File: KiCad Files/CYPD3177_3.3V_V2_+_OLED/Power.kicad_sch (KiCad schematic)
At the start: 36 parts, among them J11 USB_C_Receptacle_USB2.0_14P, J5 Conn_01x02_Pin, J6 Conn_02x02_Counter_Clockwise, J7 Conn_02x02_Counter_Clockwise, U5 TPS62933DRLR, U6 AON7534, U7 AON7534, U8 AP33772S, U9 XC6220B331PR-G

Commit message: changed pcb
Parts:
- removed H2: MountingHole, MountingHole:MountingHole_2.7mm_M2.5_DIN965_Pad_TopBottom, symbol Mechanical:MountingHole
- renumbered C16 to C10, C17 to C11, C18 to C12, C19 to C13, C20 to C14, C21 to C15, C23 to C4, C3 to C5, C24 to C6, C10 to C7, C6 to C8, C11 to C9, D5 to D3, D2 to D4, D3 to D5, J11 to J1, J5 to J2, J7 to J3, J6 to J4, L3 to L1, N22 to N1, R6 to R14, R7 to R15, R13 to R16, R12 to R17, R14 to R18, R18 to R19, R12 to R20, TH2 to TH1, U9 to U3, U5 to U4, U6 to U5, U8 to U6
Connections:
- no-connect marks 6 -> 5

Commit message: schematics done
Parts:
- removed H1: MountingHole, MountingHole:MountingHole_2.7mm_M2.5_DIN965_Pad_TopBottom, symbol Mechanical:MountingHole
- U4: footprint Power_Converter:SOT583 -> TPS62933PDRLR:SOFL50P160X60-8N
- U6: footprint Interface_USBC:QFN-24-1EP_4x4mm_P0.5mm_EP2.6x2.6mm -> Package_DFN_QFN:QFN-24-1EP_4x4mm_P0.5mm_EP2.65x2.65mm
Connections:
- no-connect marks 5 -> 4
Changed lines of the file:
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@@
 	)
 	(no_connect
-		(at 243.84 64.77)
-	)
-	(no_connect
 		(at 39.37 166.37)
 	)
@@
 			)
 		)
-		(property "Footprint" "Interface_USBC:QFN-24-1EP_4x4mm_P0.5mm_EP2.6x2.6mm"
+		(property "Footprint" "Package_DFN_QFN:QFN-24-1EP_4x4mm_P0.5mm_EP2.65x2.65mm"
 			(at 55.372 27.94 0)
 			(effects
@@
 			)
 		)
-		(property "Footprint" "Power_Converter:SOT583"
+		(property "Footprint" "TPS62933PDRLR:SOFL50P160X60-8N"
 			(at 49.53 168.91 0)
 			(effects
@@
 					(unit 1)
 				)
-			)
-		)
-	)
-	(symbol
-		(lib_id "Mechanical:MountingHole")
-		(at 243.84 64.77 0)
-		(unit 1)
-		(exclude_from_sim yes)
-		(in_bom no)
-		(on_board yes)
-		(dnp no)
-		(fields_autoplaced yes)
-		(property "Reference" "H1"
-			(at 246.38 63.4999 0)
-			(effects
-				(font
-					(size 1.27 1.27)
-				)
-				(justify left)
-			)
-		)
-		(property "Value" "MountingHole"
-			(at 246.38 66.0399 0)
-			(effects
-				(font
-					(size 1.27 1.27)
-				)
-				(justify left)
-			)
-		)
-		(property "Footprint" "MountingHole:MountingHole_2.7mm_M2.5_DIN965_Pad_TopBottom"
-			(at 243.84 64.77 0)
-			(effects
-				(font
-					(size 1.27 1.27)
-				)
-				(hide yes)
-			)
-		)
-		(property "Datasheet" "~"
-			(at 243.84 64.77 0)
-			(effects
-				(font
-					(size 1.27 1.27)
-				)
-				(hide yes)
-			)
-		)
-		(property "Description" "Mounting Hole without connection"
-			(at 243.84 64.77 0)
-			(effects
-				(font
-					(size 1.27 1.27)
-				)
-				(hide yes)
-			)
-		)
-		(instances
-			(project "CYPD3177_3.3V_V2_+_OLED"
-				(path "/a370047b-ebc6-4236-825e-9462ba7e4392/f9278a29-edee-4e3c-b24d-7a370e39fb32"
-					(reference "H1")
-					(unit 1)
-				)

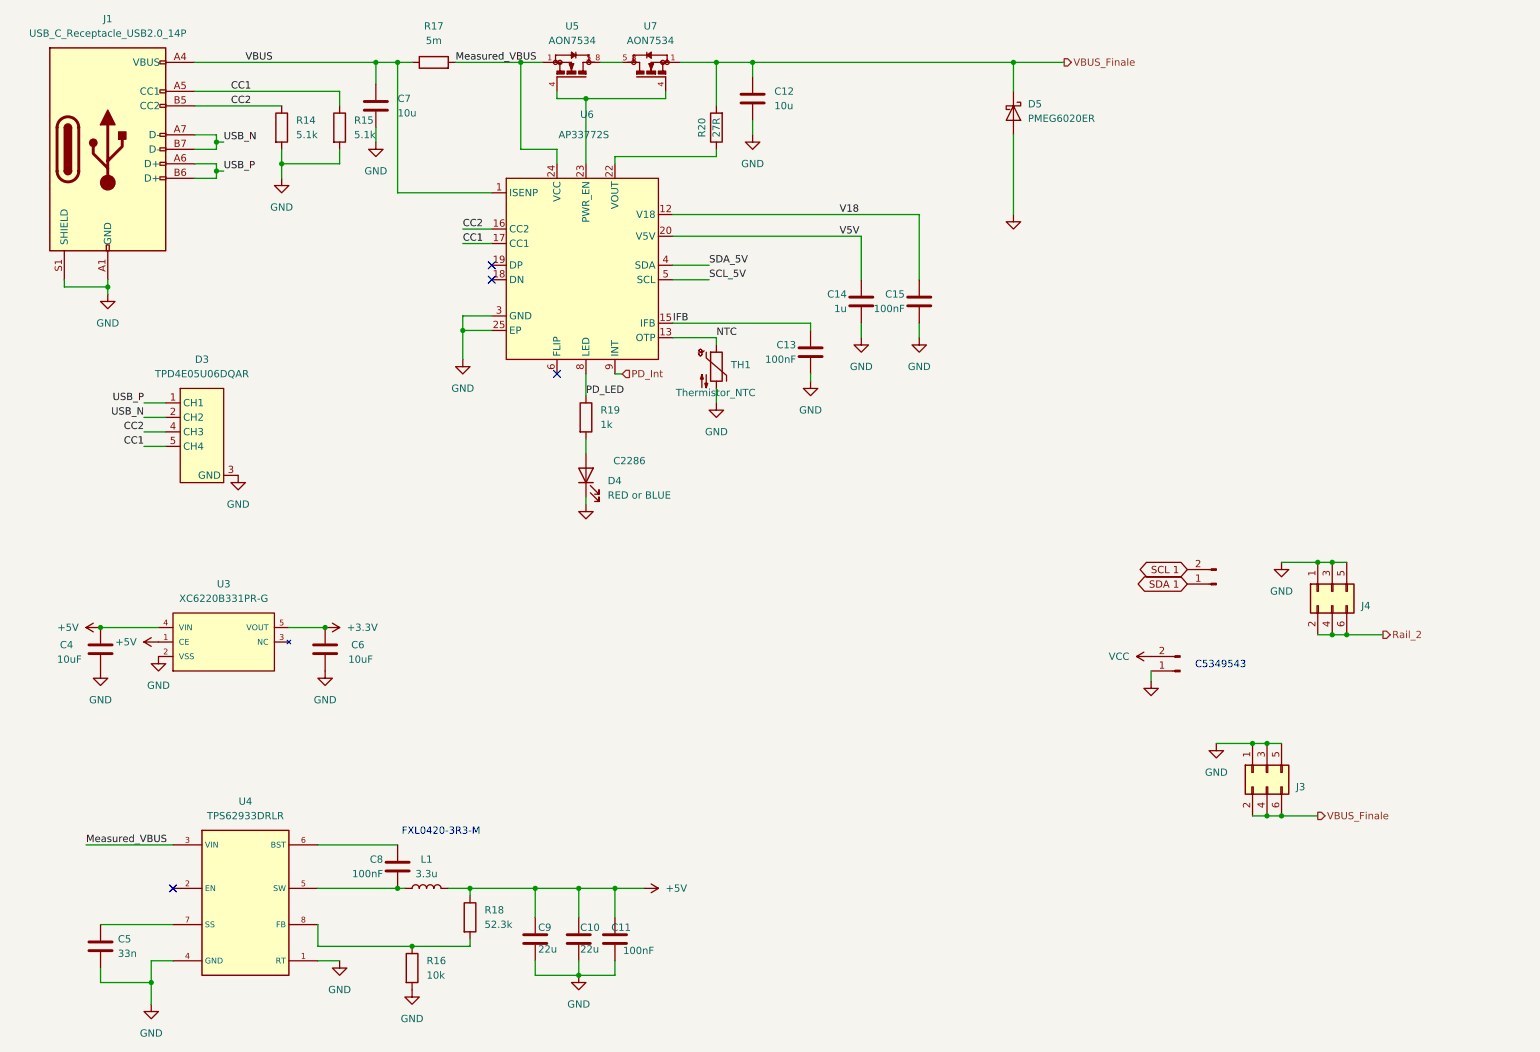
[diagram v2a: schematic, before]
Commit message: major cahnges do desing, now think final design before designing pcb
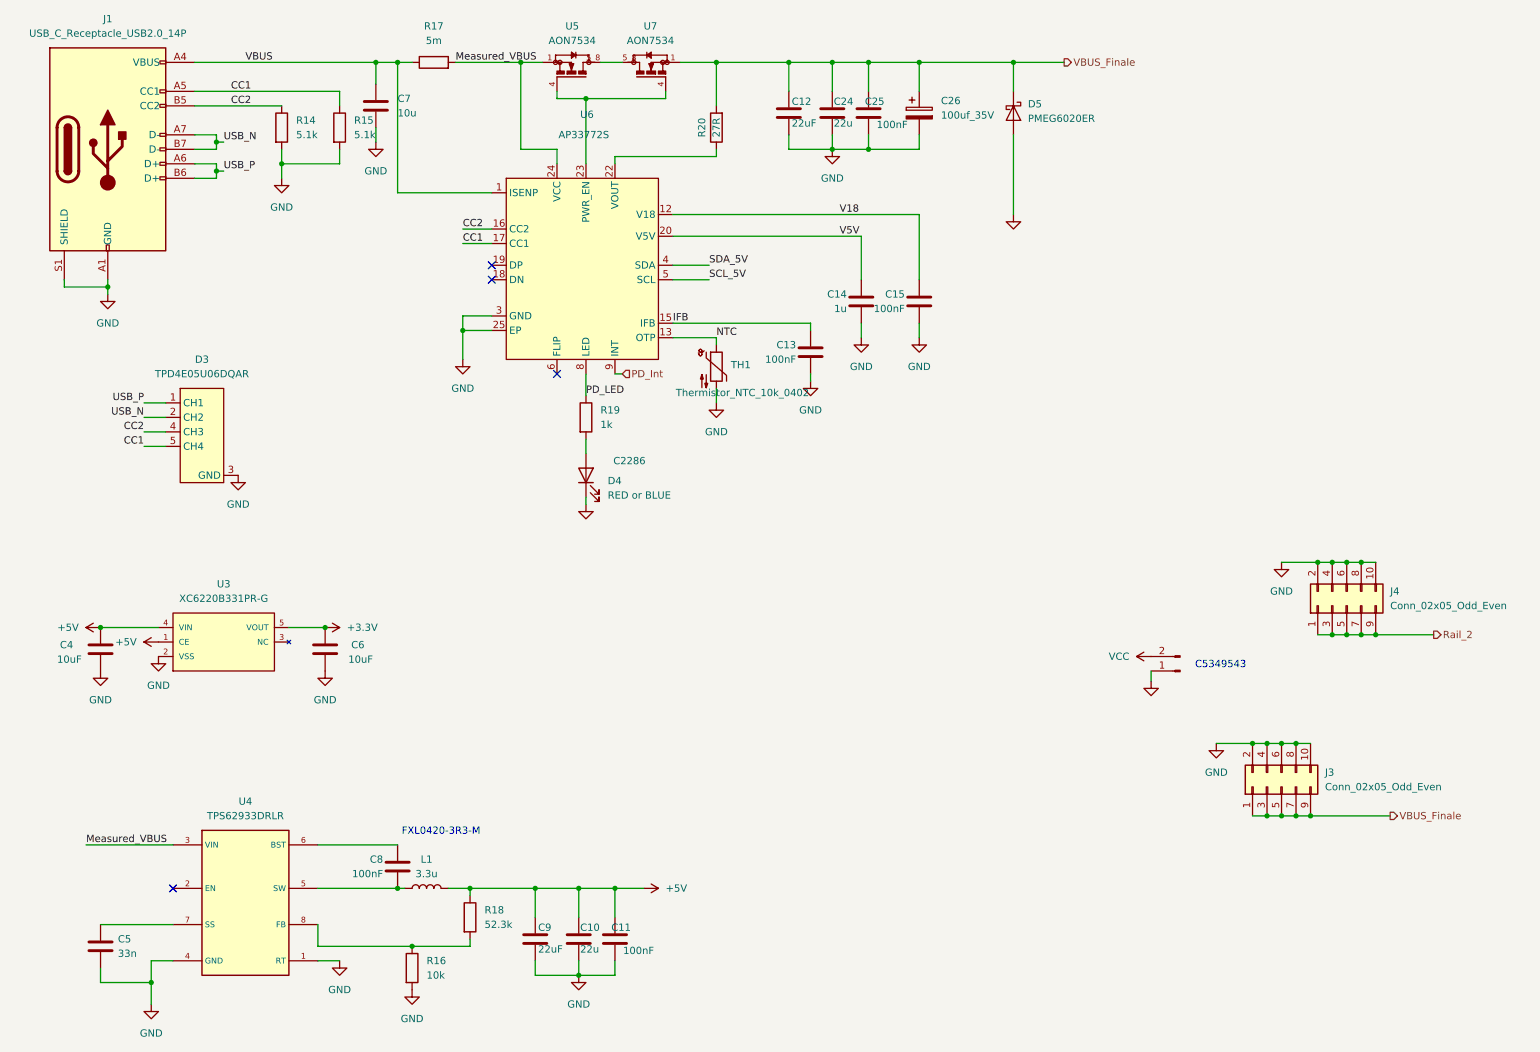
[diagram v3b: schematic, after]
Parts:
- removed J3, J4: Conn_02x02_Counter_Clockwise, Connector_PinHeader_2.54mm:PinHeader_2x03_P2.54mm_Vertical_SMD, symbol Connector_Generic:Conn_02x03_Odd_Even
- removed N1: Conn_01x02_Pin, Connector_PinHeader_2.54mm:PinHeader_1x02_P2.54mm_Vertical, symbol Connector:Conn_01x02_Pin
- added C24: 22u, Capacitor_SMD:C_1206_3216Metric, symbol Device:C
- added C25: 100nF, Capacitor_SMD:C_0402_1005Metric_Pad0.74x0.62mm_HandSolder, symbol Device:C
- added C26: 100uf_35V, Capacitor_SMD:CP_Elec_6.3x7.7, symbol Device:C_Polarized
- added J3, J4: Conn_02x05_Odd_Even, PinHeader_2x05_P2.54mm_Vertical_SMD, symbol Connector_Generic:Conn_02x05_Odd_Even
- C10: footprint Capacitor_SMD:C_0805_2012Metric -> Capacitor_SMD:C_1206_3216Metric
- C11: footprint Capacitor_SMD:C_0402_1005Metric -> Capacitor_SMD:C_0402_1005Metric_Pad0.74x0.62mm_HandSolder
- C12: value 10u -> 22uF; LCSC C513774 -> C45783
- C4, C6, C7: footprint Capacitor_SMD:C_1206_3216Metric -> Capacitor_SMD:C_0402_1005Metric_Pad0.74x0.62mm_HandSolder
- C9: value 22u -> 22uF; footprint Capacitor_SMD:C_0805_2012Metric -> Capacitor_SMD:C_1206_3216Metric
- TH1: value Thermistor_NTC -> Thermistor_NTC_10k_0402
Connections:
- net GND: now also C24.2, C25.2, C26.2, J3.10 (Pin_10), J3.2 (Pin_2), J3.4 (Pin_4), J3.6 (Pin_6), J3.8 (Pin_8), J4.10 (Pin_10), J4.2 (Pin_2), J4.4 (Pin_4), J4.6 (Pin_6), J4.8 (Pin_8)
- net Rail_2: now also J4.1 (Pin_1), J4.3 (Pin_3), J4.5 (Pin_5), J4.7 (Pin_7), J4.9 (Pin_9)
- net VBUS_Finale: now also C24.1, C25.1, C26.1, J3.1 (Pin_1), J3.3 (Pin_3), J3.5 (Pin_5), J3.7 (Pin_7), J3.9 (Pin_9)

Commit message: some changes
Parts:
- C10: value 22u -> 22uF
- C13, C15: footprint Capacitor_SMD:C_0402_1005Metric -> Capacitor_SMD:C_0402_1005Metric_Pad0.74x0.62mm_HandSolder
- C7: value 10u -> 10uF; footprint Capacitor_SMD:C_0402_1005Metric_Pad0.74x0.62mm_HandSolder -> Capacitor_SMD:C_0805_2012Metric_Pad1.18x1.45mm_HandSolder
- R17: footprint Resistor_SMD:R_0805_2012Metric -> Inductor_SMD:L_1206_3216Metric_Pad1.42x1.75mm_HandSolder
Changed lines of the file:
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@@
 			)
 		)
-		(property "Footprint" "Capacitor_SMD:C_0402_1005Metric"
+		(property "Footprint" "Capacitor_SMD:C_0402_1005Metric_Pad0.74x0.62mm_HandSolder"
 			(at 169.2148 67.31 0)
 			(effects
@@
 			)
 		)
-		(property "Value" "10u"
+		(property "Value" "10uF"
 			(at 78.74 30.4799 0)
 			(effects
@@
 			)
 		)
-		(property "Footprint" "Capacitor_SMD:C_0402_1005Metric_Pad0.74x0.62mm_HandSolder"
+		(property "Footprint" "Capacitor_SMD:C_0805_2012Metric_Pad1.18x1.45mm_HandSolder"
 			(at 75.8952 33.02 0)
 			(effects
@@
 			)
 		)
-		(property "Footprint" "Resistor_SMD:R_0805_2012Metric"
+		(property "Footprint" "Inductor_SMD:L_1206_3216Metric_Pad1.42x1.75mm_HandSolder"
 			(at 85.09 23.368 90)
 			(effects
@@
 			)
 		)
-		(property "Footprint" "Capacitor_SMD:C_0402_1005Metric"
+		(property "Footprint" "Capacitor_SMD:C_0402_1005Metric_Pad0.74x0.62mm_HandSolder"
 			(at 150.1648 76.2 0)
 			(effects
@@
 			)
 		)
-		(property "Value" "22u"
+		(property "Value" "22uF"
 			(at 110.744 177.038 0)
 			(effects

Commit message: changes
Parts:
- C14: footprint Capacitor_SMD:C_0603_1608Metric -> Capacitor_SMD:C_0402_1005Metric_Pad0.74x0.62mm_HandSolder
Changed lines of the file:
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@@
 			)
 		)
-		(property "Footprint" "Capacitor_SMD:C_0603_1608Metric"
+		(property "Footprint" "Capacitor_SMD:C_0402_1005Metric_Pad0.74x0.62mm_HandSolder"
 			(at 159.0548 67.31 0)
 			(effects

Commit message: s
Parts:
- added C27: 10uF, Capacitor_SMD:C_1206_3216Metric, symbol Device:C
- C5: value 33n -> 33nF; footprint Capacitor_SMD:C_0603_1608Metric -> Resistor_SMD:R_0402_1005Metric
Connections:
- net GND: now also C27.2
- net Measured_VBUS: now also C27.1
- net SCL_5V renamed SDA
- net SDA_5V renamed SCL
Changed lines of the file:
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@@
 	)
 	(junction
+		(at 30.48 158.75)
+		(diameter 0)
+		(color 0 0 0 0)
+	)
+	(junction
 		(at 26.67 120.65)
 		(diameter 0)
@@
 	(wire
 		(pts
-			(xy 24.13 158.75) (xy 39.37 158.75)
+			(xy 24.13 158.75) (xy 30.48 158.75)
 		)
 		(stroke
@@
 	(wire
 		(pts
+			(xy 30.48 158.75) (xy 39.37 158.75)
+		)
+		(stroke
+			(width 0)
+			(type default)
+		)
+	)
+	(wire
+		(pts
 			(xy 231.14 153.67) (xy 233.68 153.67)
 		)
@@
 		)
 	)
-	(label "SCL_5V"
-		(at 133.35 59.69 0)
-		(effects
-			(font
-				(size 1.27 1.27)
-			)
-			(justify left bottom)
-		)
-	)
 	(label "CC2"
 		(at 49.53 29.21 0)
@@
 		)
 	)
-	(label "SDA_5V"
-		(at 133.35 57.15 0)
-		(effects
-			(font
-				(size 1.27 1.27)
-			)
-			(justify left bottom)
-		)
-	)
 	(label "CC1"
 		(at 49.53 26.67 0)
@@
 		)
 	)
+	(hierarchical_label "SCL"
+		(shape bidirectional)
+		(at 133.35 57.15 0)
+		(effects
+			(font
+				(size 1.27 1.27)
+			)
+			(justify left)
+		)
+	)
+	(hierarchical_label "SDA"
+		(shape bidirectional)
+		(at 133.35 59.69 0)
+		(effects
+			(font
+				(size 1.27 1.27)
+			)
+			(justify left)
+		)
+	)
 	(symbol
 		(lib_id "Device:C")
@@
 	(symbol
 		(lib_id "Device:C")
+		(at 30.48 162.56 0)
+		(unit 1)
+		(exclude_from_sim no)
+		(in_bom yes)
+		(on_board yes)
+		(dnp no)
+		(property "Reference" "C27"
+			(at 30.988 160.528 0)
+			(effects
+				(font
+					(size 1.27 1.27)
+				)
+				(justify left)
+			)
+		)
+		(property "Value" "10uF"
+			(at 30.988 164.338 0)
+			(effects
+				(font
+					(size 1.27 1.27)
+				)
+				(justify left)
+			)
+		)
+		(property "Footprint" "Capacitor_SMD:C_1206_3216Metric"
+			(at 31.4452 166.37 0)
+			(effects
+				(font
+					(size 1.27 1.27)
+				)
+				(hide yes)
+			)
+		)
+		(property "Datasheet" "https://www.lcsc.com/datasheet/lcsc_datasheet_2005191033_Samwha-Capacitor-CS3216X5R106K500NRI_C513774.pdf"
+			(at 30.48 162.56 0)
+			(effects
+				(font
+					(size 1.27 1.27)
+				)
+				(hide yes)
+			)
+		)
+		(property "Description" "Unpolarized capacitor"
+			(at 30.48 162.56 0)
+			(effects
+				(font
+					(size 1.27 1.27)
+				)
+				(hide yes)
+			)
+		)
+		(property "LCSC" "C45783"
+			(at 30.48 162.56 0)
+			(effects
+				(font
+					(size 1.27 1.27)
+				)
+				(hide yes)
+			)
+		)
+		(pin "1"
+		)
+		(pin "2"
+		)
+		(instances
+			(project "CYPD3177_3.3V_V2_+_OLED"
+				(path "/a370047b-ebc6-4236-825e-9462ba7e4392/f9278a29-edee-4e3c-b24d-7a370e39fb32"
+					(reference "C27")
+					(unit 1)
+				)
+			)
+		)
+	)
+	(symbol
+		(lib_id "Device:C")
 		(at 116.84 175.26 0)
 		(mirror y)
@@
 	)
 	(symbol
+		(lib_id "power:GND")
+		(at 30.48 166.37 0)
+		(unit 1)
+		(exclude_from_sim no)
+		(in_bom yes)
+		(on_board yes)
+		(dnp no)
+		(property "Reference" "#PWR085"
+			(at 30.48 172.72 0)
+			(effects
+				(font
+					(size 1.27 1.27)
+				)
+				(hide yes)
+			)
+		)
+		(property "Value" "GND"
+			(at 26.924 168.402 0)
+			(effects
+				(font
+					(size 1.27 1.27)
+				)
+			)
+		)
+		(property "Footprint" ""
+			(at 30.48 166.37 0)
+			(effects
+				(font
+					(size 1.27 1.27)
+				)
+				(hide yes)
+			)
+		)
+		(property "Datasheet" ""
+			(at 30.48 166.37 0)
+			(effects
+				(font
+					(size 1.27 1.27)
+				)
+				(hide yes)
+			)
+		)
+		(property "Description" "Power symbol creates a global label with name \"GND\" , ground"
+			(at 30.48 166.37 0)
+			(effects
+				(font
+					(size 1.27 1.27)
+				)
+				(hide yes)
+			)
+		)
+		(pin "1"
+		)
+		(instances
+			(project "CYPD3177_3.3V_V2_+_OLED"
+				(path "/a370047b-ebc6-4236-825e-9462ba7e4392/f9278a29-edee-4e3c-b24d-7a370e39fb32"
+					(reference "#PWR085")
+					(unit 1)
+				)
+			)
+		)
+	)
+	(symbol
 		(lib_id "Device:C")
 		(at 147.32 30.48 0)
@@
 			)
 		)
-		(property "Value" "33n"
+		(property "Value" "33nF"
 			(at 29.718 177.8 0)
 			(effects
@@
 			)
 		)
-		(property "Footprint" "Capacitor_SMD:C_0603_1608Metric"
+		(property "Footprint" "Resistor_SMD:R_0402_1005Metric"
 			(at 27.6352 180.34 0)
 			(effects

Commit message: changes
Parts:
- C11, C25, C4, C6: footprint Capacitor_SMD:C_0402_1005Metric_Pad0.74x0.62mm_HandSolder -> Capacitor_SMD:C_0402_1005Metric
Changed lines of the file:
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@@
 			)
 		)
-		(property "Footprint" "Capacitor_SMD:C_0402_1005Metric_Pad0.74x0.62mm_HandSolder"
+		(property "Footprint" "Capacitor_SMD:C_0402_1005Metric"
 			(at 115.8748 179.07 0)
 			(effects
@@
 			)
 		)
-		(property "Footprint" "Capacitor_SMD:C_0402_1005Metric_Pad0.74x0.62mm_HandSolder"
+		(property "Footprint" "Capacitor_SMD:C_0402_1005Metric"
 			(at 160.3248 34.29 0)
 			(effects
@@
 			)
 		)
-		(property "Footprint" "Capacitor_SMD:C_0402_1005Metric_Pad0.74x0.62mm_HandSolder"
+		(property "Footprint" "Capacitor_SMD:C_0402_1005Metric"
 			(at 27.6352 128.27 0)
 			(effects
@@
 			)
 		)
-		(property "Footprint" "Capacitor_SMD:C_0402_1005Metric_Pad0.74x0.62mm_HandSolder"
+		(property "Footprint" "Capacitor_SMD:C_0402_1005Metric"
 			(at 67.0052 128.27 0)
 			(effects

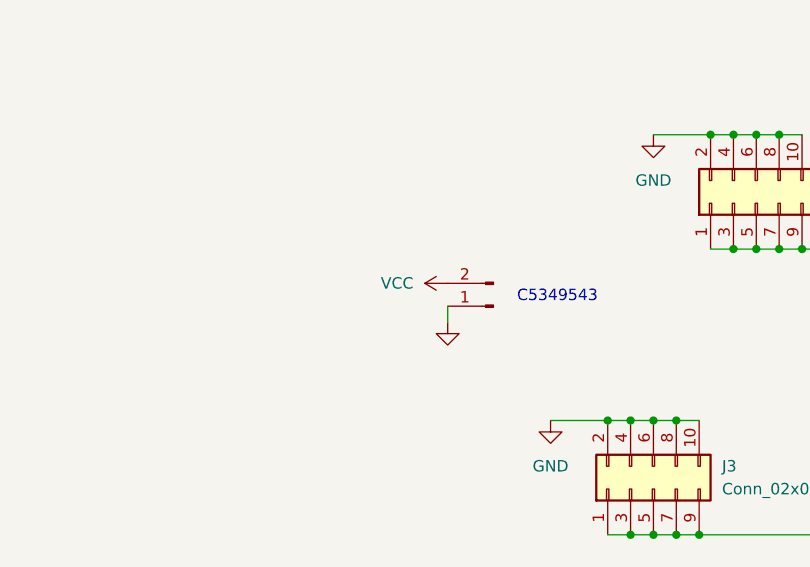
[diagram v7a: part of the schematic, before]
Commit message: CYPD3177 wiring finshed, only silkscreen needs changes and make a breakout board
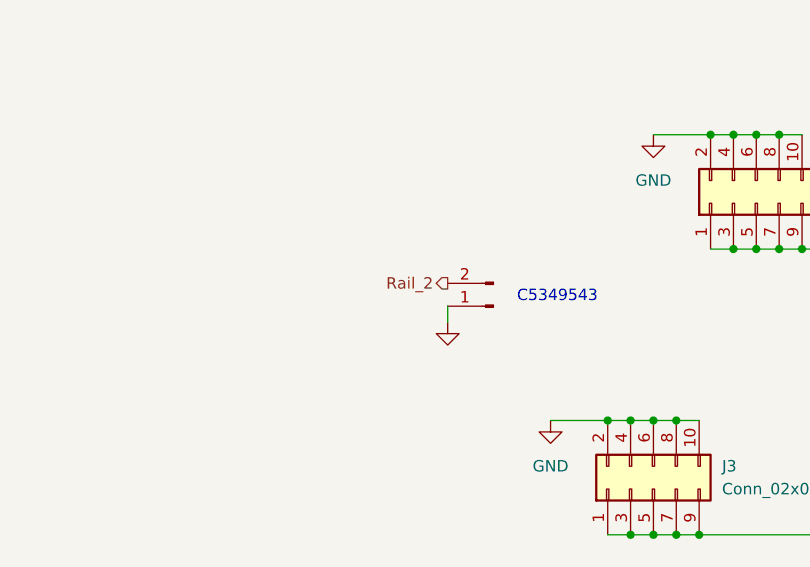
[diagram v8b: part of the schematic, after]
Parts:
- C13, C14, C15: footprint Capacitor_SMD:C_0402_1005Metric_Pad0.74x0.62mm_HandSolder -> Capacitor_SMD:C_0402_1005Metric
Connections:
- net VCC is gone; now on net Rail_2: J2.2 (Pin_2)
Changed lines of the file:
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@@
 		)
 	)
+	(hierarchical_label "Rail_2"
+		(shape output)
+		(at 210.82 125.73 180)
+		(effects
+			(font
+				(size 1.27 1.27)
+			)
+			(justify right)
+		)
+	)
 	(hierarchical_label "VBUS_Finale"
 		(shape output)
@@
 			)
 		)
-		(property "Footprint" "Capacitor_SMD:C_0402_1005Metric_Pad0.74x0.62mm_HandSolder"
+		(property "Footprint" "Capacitor_SMD:C_0402_1005Metric"
 			(at 169.2148 67.31 0)
 			(effects
@@
 	)
 	(symbol
-		(lib_id "power:VCC")
-		(at 210.82 125.73 90)
-		(unit 1)
-		(exclude_from_sim no)
-		(in_bom yes)
-		(on_board yes)
-		(dnp no)
-		(fields_autoplaced yes)
-		(property "Reference" "#PWR048"
-			(at 214.63 125.73 0)
-			(effects
-				(font
-					(size 1.27 1.27)
-				)
-				(hide yes)
-			)
-		)
-		(property "Value" "VCC"
-			(at 207.01 125.7299 90)
-			(effects
-				(font
-					(size 1.27 1.27)
-				)
-				(justify left)
-			)
-		)
-		(property "Footprint" ""
-			(at 210.82 125.73 0)
-			(effects
-				(font
-					(size 1.27 1.27)
-				)
-				(hide yes)
-			)
-		)
-		(property "Datasheet" ""
-			(at 210.82 125.73 0)
-			(effects
-				(font
-					(size 1.27 1.27)
-				)
-				(hide yes)
-			)
-		)
-		(property "Description" "Power symbol creates a global label with name \"VCC\""
-			(at 210.82 125.73 0)
-			(effects
-				(font
-					(size 1.27 1.27)
-				)
-				(hide yes)
-			)
-		)
-		(pin "1"
-		)
-		(instances
-			(project "CYPD3177_3.3V_V2_+_OLED"
-				(path "/a370047b-ebc6-4236-825e-9462ba7e4392/f9278a29-edee-4e3c-b24d-7a370e39fb32"
-					(reference "#PWR048")
-					(unit 1)
-				)
-			)
-		)
-	)
-	(symbol
 		(lib_id "power:GND")
 		(at 36.83 125.73 0)
@@
 			)
 		)
-		(property "Footprint" "Capacitor_SMD:C_0402_1005Metric_Pad0.74x0.62mm_HandSolder"
+		(property "Footprint" "Capacitor_SMD:C_0402_1005Metric"
 			(at 150.1648 76.2 0)
 			(effects
@@
 			)
 		)
-		(property "Footprint" "Capacitor_SMD:C_0402_1005Metric_Pad0.74x0.62mm_HandSolder"
+		(property "Footprint" "Capacitor_SMD:C_0402_1005Metric"
 			(at 159.0548 67.31 0)
 			(effects
